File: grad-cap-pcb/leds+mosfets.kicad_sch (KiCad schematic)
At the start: 189 parts, among them T1 PHPT610035PKX, T2 PHPT610035PKX, T3 PHPT610035PKX, T4 PHPT610035PKX, T5 PHPT610035PKX, T6 PHPT610035PKX, T7 PHPT610035PKX, T8 PHPT610035PKX, U1 CD4072BM96, U2 CD4075BM96, U3 SN74AHCT32DBR, U6 SN74AHCT32DBR, U8 SN74AHCT32DBR

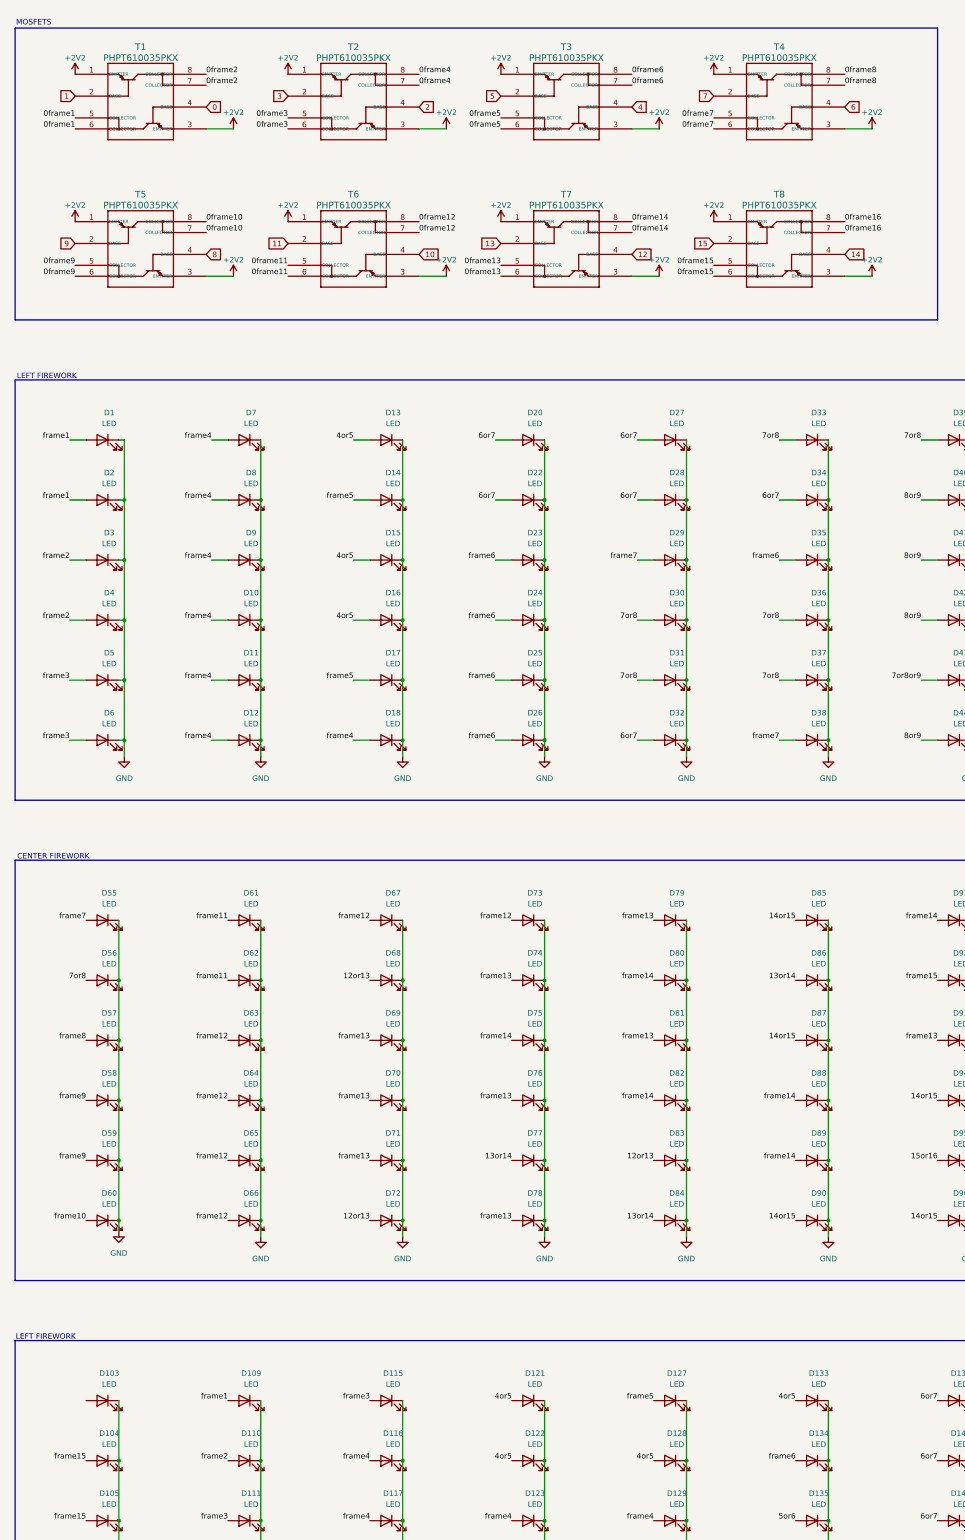
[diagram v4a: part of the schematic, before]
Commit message: screw it were making it 8 frames, 16 is too mcuh
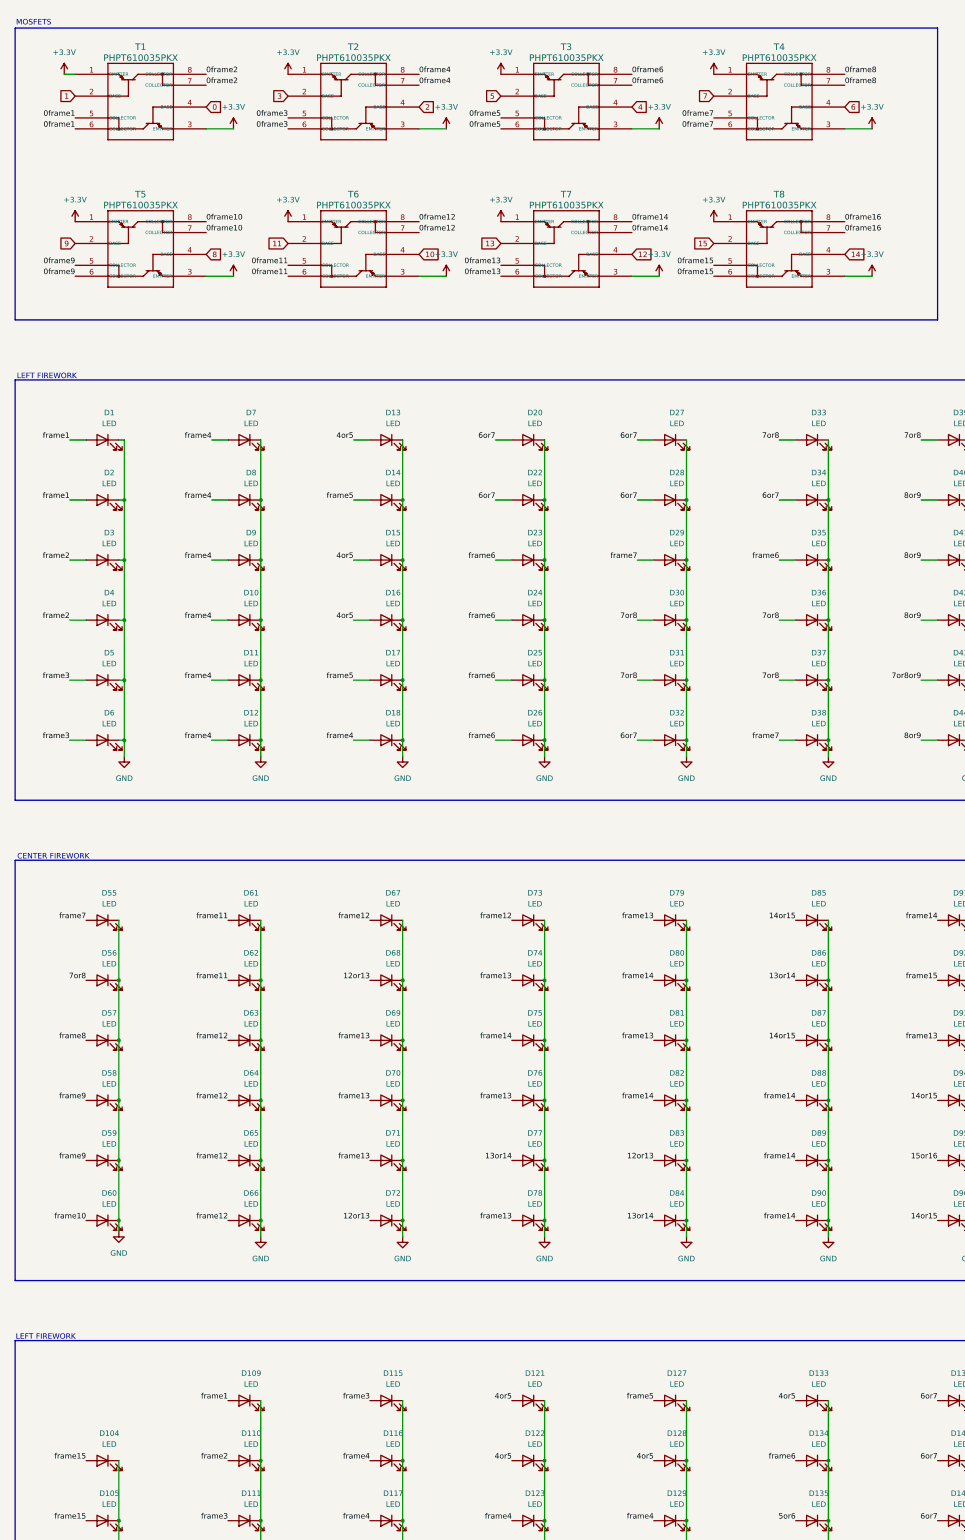
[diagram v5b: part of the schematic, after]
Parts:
- removed D103: LED, LED_SMD:LED_0603_1608Metric, symbol Device:LED
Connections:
- net +2V2 is gone; now on net +3.3V: T1.1 (EMITTER), T1.3 (EMITTER), T2.1 (EMITTER), T2.3 (EMITTER), T3.1 (EMITTER), T3.3 (EMITTER), T4.1 (EMITTER), T4.3 (EMITTER), T5.1 (EMITTER), T5.3 (EMITTER), T6.1 (EMITTER), T6.3 (EMITTER), T7.1 (EMITTER), T7.3 (EMITTER), T8.1 (EMITTER), T8.3 (EMITTER)
- net 14or15: no longer D90.2 (A)
- net frame14: now also D90.2 (A)
